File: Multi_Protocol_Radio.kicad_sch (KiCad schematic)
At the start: 9 parts, among them J2001 Conn_02x06_Odd_Even, J2004 Conn_02x06_Odd_Even, U2001 MGM240PB32VNA3, U2002 Mini_Simplicity_Connector_(10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

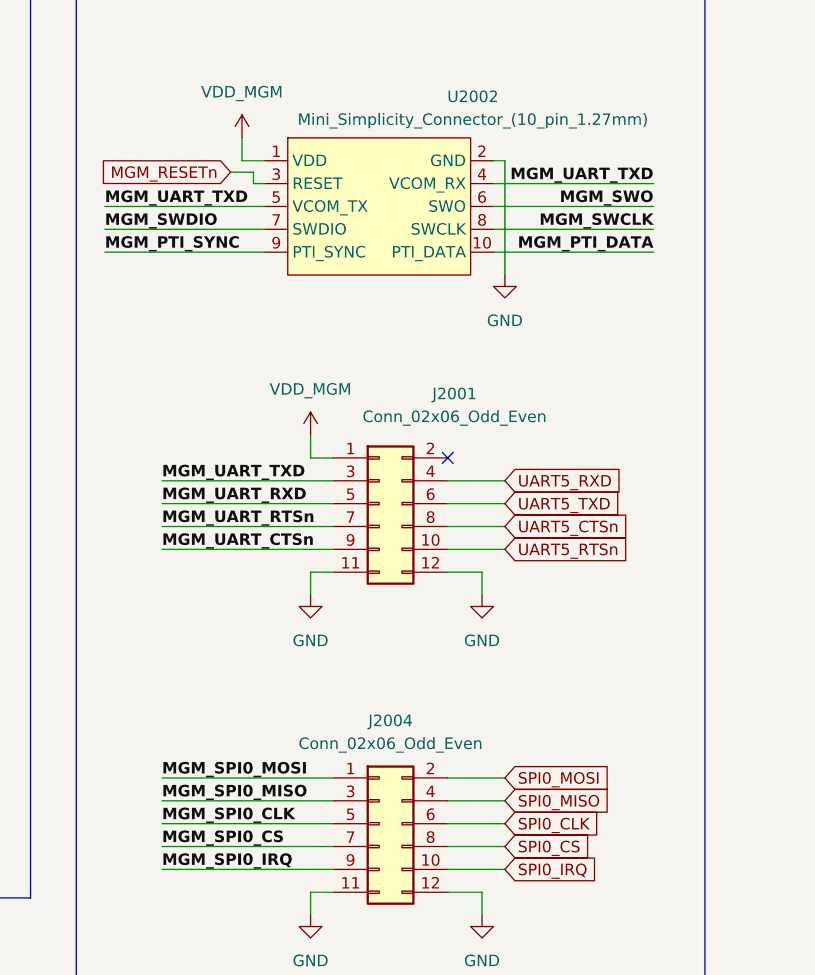
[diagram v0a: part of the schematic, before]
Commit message: Placed and routed new UART and SPI headers, routed out correct MGM240P pinout, routed out Mini Simplicity 10 pin connector, swapped legless TC2050 footprint for legged version. Need to reroute SoC JTAG
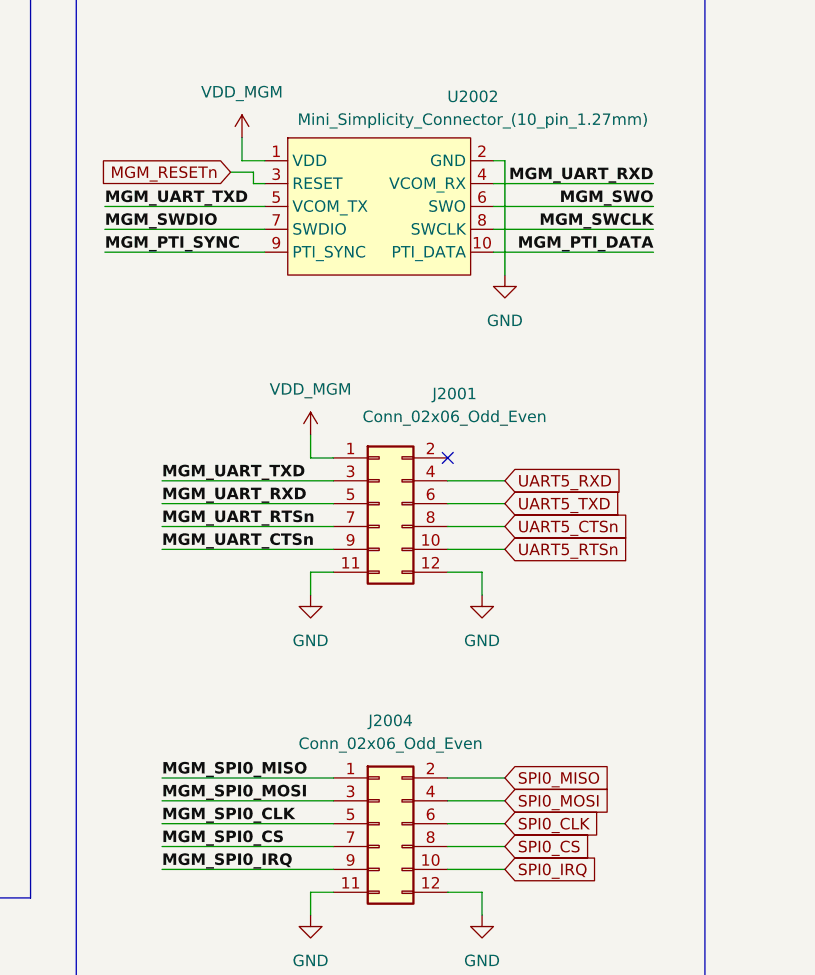
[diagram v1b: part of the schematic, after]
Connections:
- net MGM_SPI0_MISO: now also J2004.1 (Pin_1); no longer J2004.3 (Pin_3)
- net MGM_SPI0_MOSI: now also J2004.3 (Pin_3); no longer J2004.1 (Pin_1)
- net MGM_UART_RXD: now also U2002.4 (VCOM_RX)
- net MGM_UART_TXD: no longer U2002.4 (VCOM_RX)
- net SPI0_MISO: now also J2004.2 (Pin_2); no longer J2004.4 (Pin_4)
- net SPI0_MOSI: now also J2004.4 (Pin_4); no longer J2004.2 (Pin_2)
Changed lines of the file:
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@@
 		)
 	)
-	(label "MGM_UART_TXD"
+	(label "MGM_UART_RXD"
 		(at 220.98 80.01 180)
 		(effects
@@
 	)
 	(label "MGM_SPI0_MISO"
-		(at 166.37 148.59 0)
+		(at 166.37 146.05 0)
 		(effects
 			(font
@@
 	)
 	(label "MGM_SPI0_MOSI"
-		(at 166.37 146.05 0)
+		(at 166.37 148.59 0)
 		(effects
 			(font
@@
 	(global_label "SPI0_MISO"
 		(shape input)
-		(at 204.47 148.59 0)
+		(at 204.47 146.05 0)
 		(fields_autoplaced yes)
 		(effects
@@
 		)
 		(property "Intersheetrefs" "${INTERSHEET_REFS}"
-			(at 217.3128 148.59 0)
+			(at 217.3128 146.05 0)
 			(effects
 				(font
@@
 	(global_label "SPI0_MOSI"
 		(shape input)
-		(at 204.47 146.05 0)
+		(at 204.47 148.59 0)
 		(fields_autoplaced yes)
 		(effects
@@
 		)
 		(property "Intersheetrefs" "${INTERSHEET_REFS}"
-			(at 217.3128 146.05 0)
+			(at 217.3128 148.59 0)
 			(effects
 				(font

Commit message: Ordered Rev B
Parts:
- J2001, J2004: JLCPCB Part# (none) -> C7501277
- U2002: JLCPCB Part# (none) -> C5155080
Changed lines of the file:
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@@
+			)
+		)
+		(property "JLCPCB Part#" "C7501277"
+			(at 190.5 115.57 0)
+			(effects
+				(font
+					(size 1.27 1.27)
+				)
 			)
 		)
@@
 			)
 		)
+		(property "JLCPCB Part#" "C5155080"
+			(at 190.5 82.55 0)
+			(effects
+				(font
+					(size 1.27 1.27)
+				)
+			)
+		)
 		(pin "4"
 		)
@@
 			)
 		)
+		(property "JLCPCB Part#" "C7501277"
+			(at 190.5 151.13 0)
+			(effects
+				(font
+					(size 1.27 1.27)
+				)
+			)
+		)
